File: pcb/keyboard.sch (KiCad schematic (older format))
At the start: 67 parts, among them SW1 SW_Push

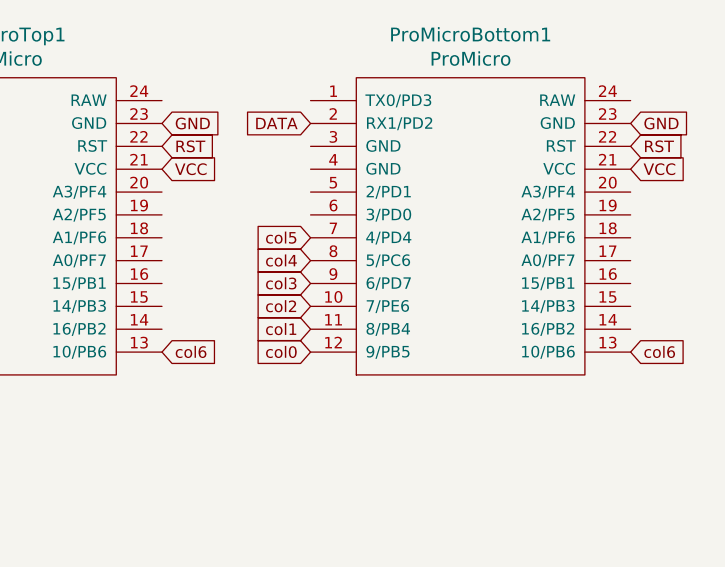
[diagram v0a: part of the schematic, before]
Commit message: Added traces for rows (kinda important ;_;)
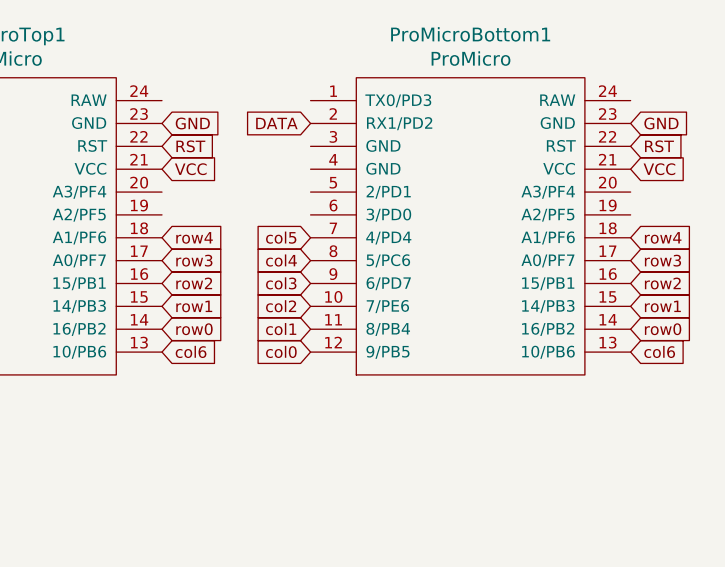
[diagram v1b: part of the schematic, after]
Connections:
- net row0: now also ProMicroBottom1.14 (16/PB2), ProMicroTop1.14 (16/PB2)
- net row1: now also ProMicroBottom1.15 (14/PB3), ProMicroTop1.15 (14/PB3)
- net row2: now also ProMicroBottom1.16 (15/PB1), ProMicroTop1.16 (15/PB1)
- net row3: now also ProMicroBottom1.17 (A0/PF7), ProMicroTop1.17 (A0/PF7)
- net row4: now also ProMicroBottom1.18 (A1/PF6), ProMicroTop1.18 (A1/PF6)
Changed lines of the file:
@@
 Text GLabel 11850 3350 2    50   Input ~ 0
 RST
+Text GLabel 9800 4150 2    50   Input ~ 0
+row0
+Text GLabel 9800 4050 2    50   Input ~ 0
+row1
+Text GLabel 9800 3950 2    50   Input ~ 0
+row2
+Text GLabel 9800 3850 2    50   Input ~ 0
+row3
+Text GLabel 9800 3750 2    50   Input ~ 0
+row4
+Text GLabel 11850 4150 2    50   Input ~ 0
+row0
+Text GLabel 11850 4050 2    50   Input ~ 0
+row1
+Text GLabel 11850 3950 2    50   Input ~ 0
+row2
+Text GLabel 11850 3850 2    50   Input ~ 0
+row3
+Text GLabel 11850 3750 2    50   Input ~ 0
+row4
 $EndSCHEMATC
